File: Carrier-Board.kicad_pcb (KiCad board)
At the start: 4 copper layers, 92 x 96 mm, 46 parts, among them J1 CONN_3-6318491-6, J10 Conn_02x03_Odd_Even, J2 Conn_01x0, J3 Conn_02x26_Odd_Even, J4 SI-51009-F, J5 Conn_02x26_Odd_Even, J6 Conn_01x03_Male, J7 Conn_01x03_Male, J8 Conn_01x06_Male, J9 Conn_02x04_Odd_Even, SW1 SW_Push, SW2 SW_Push, SW3 SW_Push, U1 MPM3620, U2 MPM3620, U9 MSATA-Socket

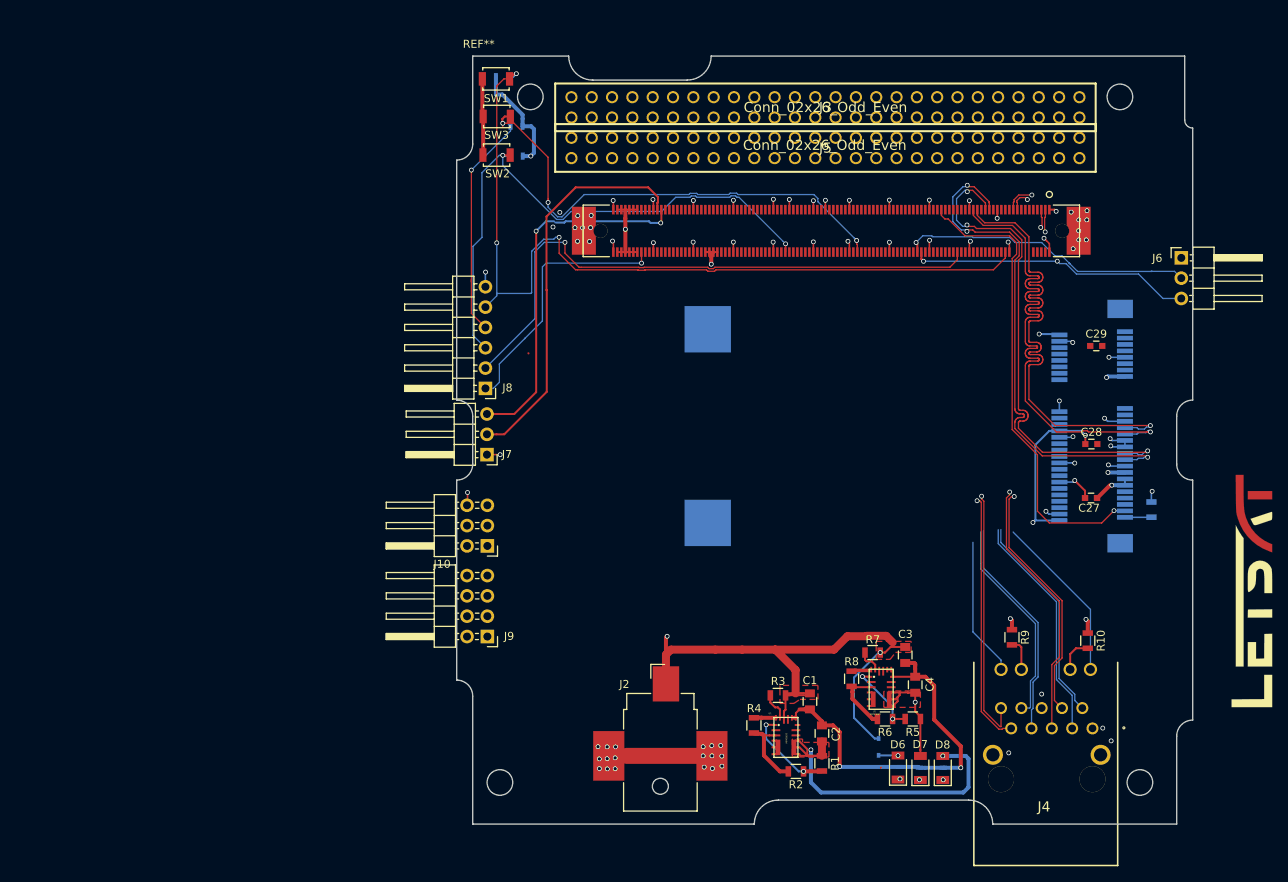
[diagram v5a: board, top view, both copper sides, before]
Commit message: Finished Traces
No camera
needs verification
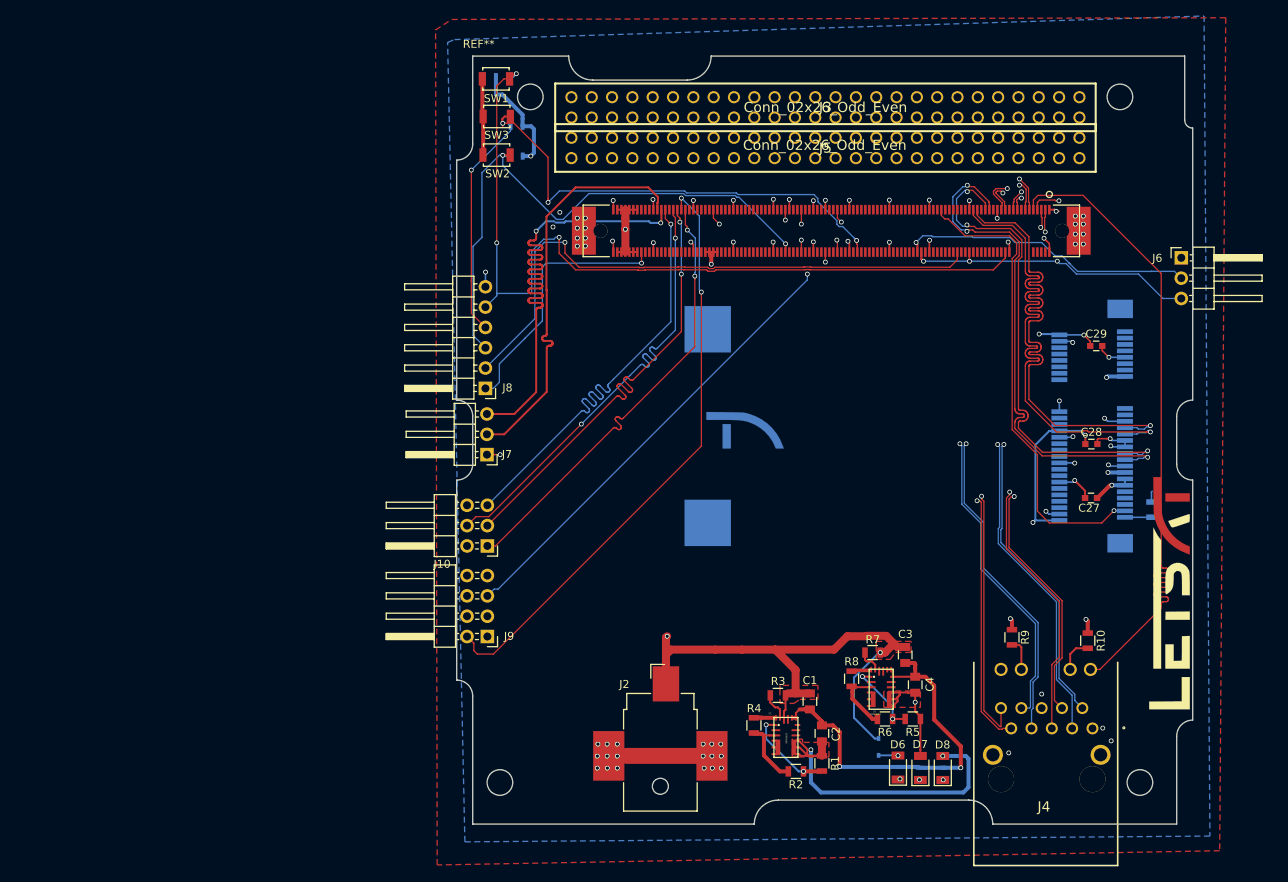
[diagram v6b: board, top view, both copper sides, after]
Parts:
- added G1: LOGO, BusSimulator:LetSatLogo440, B.Cu at (127.5, 70.8)
- moved G1 10.3 mm to (171.2, 91.0)
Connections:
- J10 pad 2: SPI_POWER -> +3.3V
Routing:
- net +3.3V: track 119.0 -> 201.9 mm, vias 5 -> 6
- net GPO2: track 0.00 -> 75.2 mm, vias 0 -> 1
- net GPI0: track 0.00 -> 75.1 mm, vias 0 -> 1
- net GPI1: track 0.00 -> 75.1 mm, vias 0 -> 1
- net GPO3: track 0.00 -> 75.1 mm, vias 0 -> 1
- net GPO1: track 0.00 -> 75.0 mm, vias 0 -> 1
- net GPI3: track 0.00 -> 75.0 mm, vias 0 -> 1
- net GPO0: track 0.00 -> 75.0 mm, vias 0 -> 2
- net GBE0_LINK100#: track 17.3 -> 86.0 mm, vias 0 -> 1
- net GPI2: track 0.00 -> 66.8 mm, vias 0 -> 2
- net GBE0_LINK1000#: track 21.2 -> 86.0 mm
- net SPI_MOSI: track 0.00 -> 56.0 mm, vias 0 -> 2
- net SPI_CS#: track 0.00 -> 56.0 mm, vias 0 -> 1
- net SPI_CLK: track 0.00 -> 56.0 mm, vias 0 -> 2
- net SPI_MISO: track 0.00 -> 56.0 mm, vias 0 -> 2
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- added copper zone on B.Cu, net GBE0_CTREF(GND)
- added copper zone on F.Cu, net GBE0_CTREF(GND)
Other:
- board text added: "S/N: 00000000"
- board text added: "mCOM-TK1 Carrier Board"

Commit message: added mounting holes
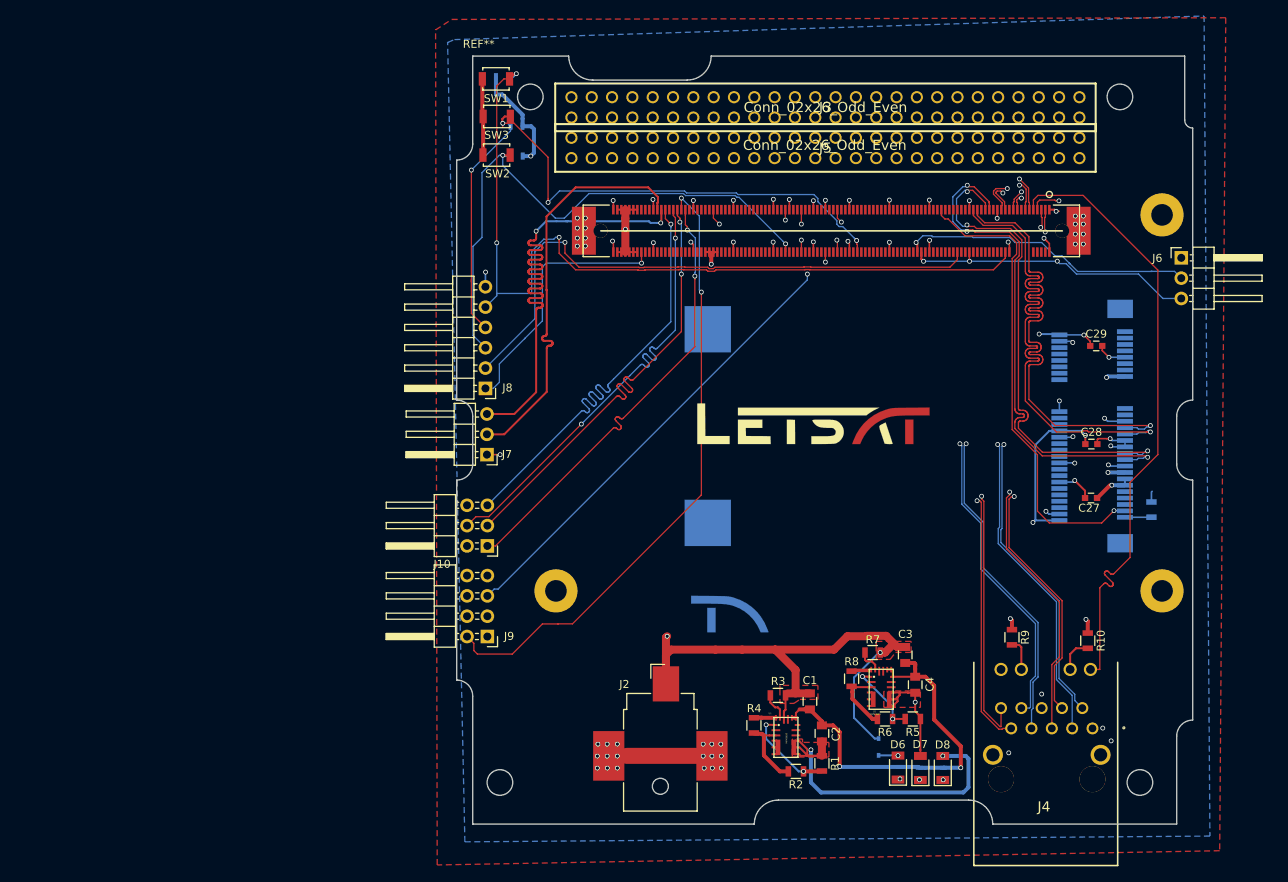
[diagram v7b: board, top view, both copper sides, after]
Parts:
- added m1: MountingHole_2.7mm_M2.5_Pad, Mounting_Holes:MountingHole_2.7mm_M2.5_Pad, F.Cu at (170.1, 43.9)
- added m1: MountingHole_2.7mm_M2.5_Pad, Mounting_Holes:MountingHole_2.7mm_M2.5_Pad, F.Cu at (170.1, 90.8)
- added m2: MountingHole_2.7mm_M2.5_Pad, Mounting_Holes:MountingHole_2.7mm_M2.5_Pad, F.Cu at (94.3, 90.8)
- moved G1 49.2 mm to (126.7, 70.2), turned to 0 degrees
- moved G1 23.0 mm to (125.6, 93.7)
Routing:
- net GPI0: track 75.1 -> 84.5 mm
- net GBE0_LINK100#: track 86.0 -> 78.0 mm
- net GBE0_LINK1000#: track 86.0 -> 78.0 mm
- net GBE0_CTREF(GND): track 160.2 -> 166.6 mm
- net (no net): track 6.33 -> 0.00 mm, vias 2 -> 0
- net GPO1: track 75.0 -> 80.5 mm
- net GPO0: track 75.0 -> 78.6 mm
- net +3.3V: track 201.9 -> 203.6 mm
